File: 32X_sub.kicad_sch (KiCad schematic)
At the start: 103 parts, among them IC511 315-5684, IC512 315-5788, IC515 74HC74, IC516 74LS00, T520 TestPoint, T526 TestPoint, T527 TestPoint, T528 TestPoint, T547 TestPoint, T548 TestPoint, T555 TestPoint, T599 AS, X501 *3

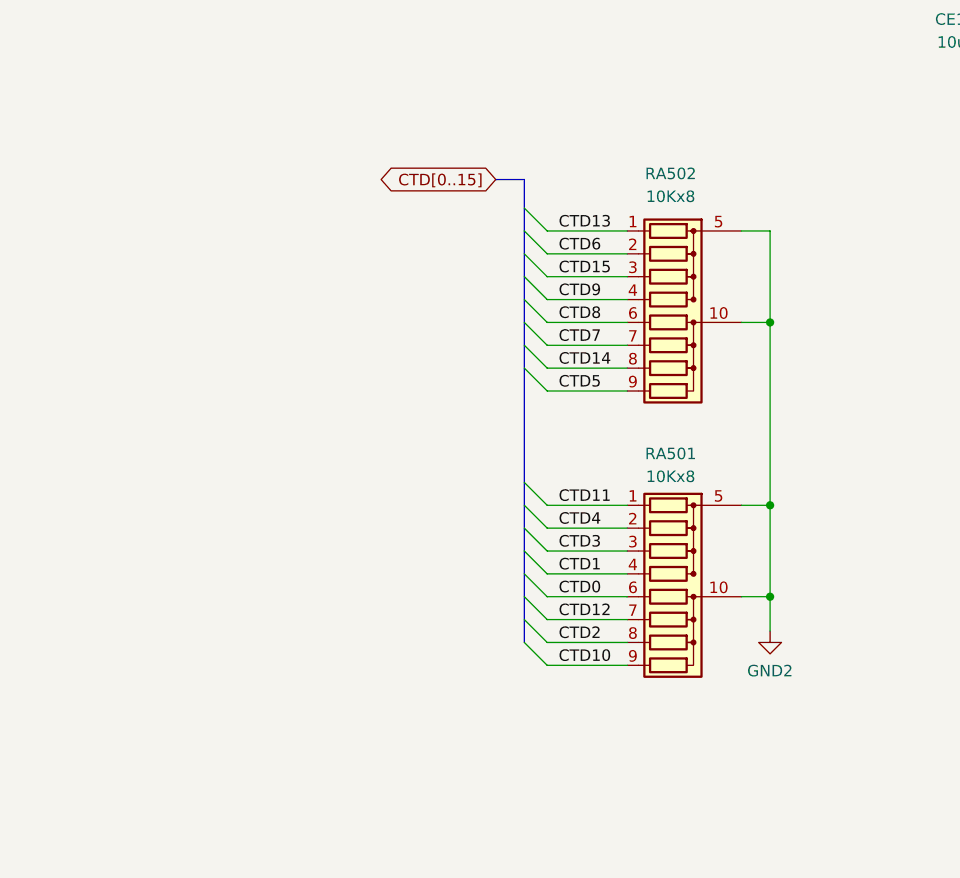
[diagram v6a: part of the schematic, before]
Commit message: Use more readily-available resistor packs.
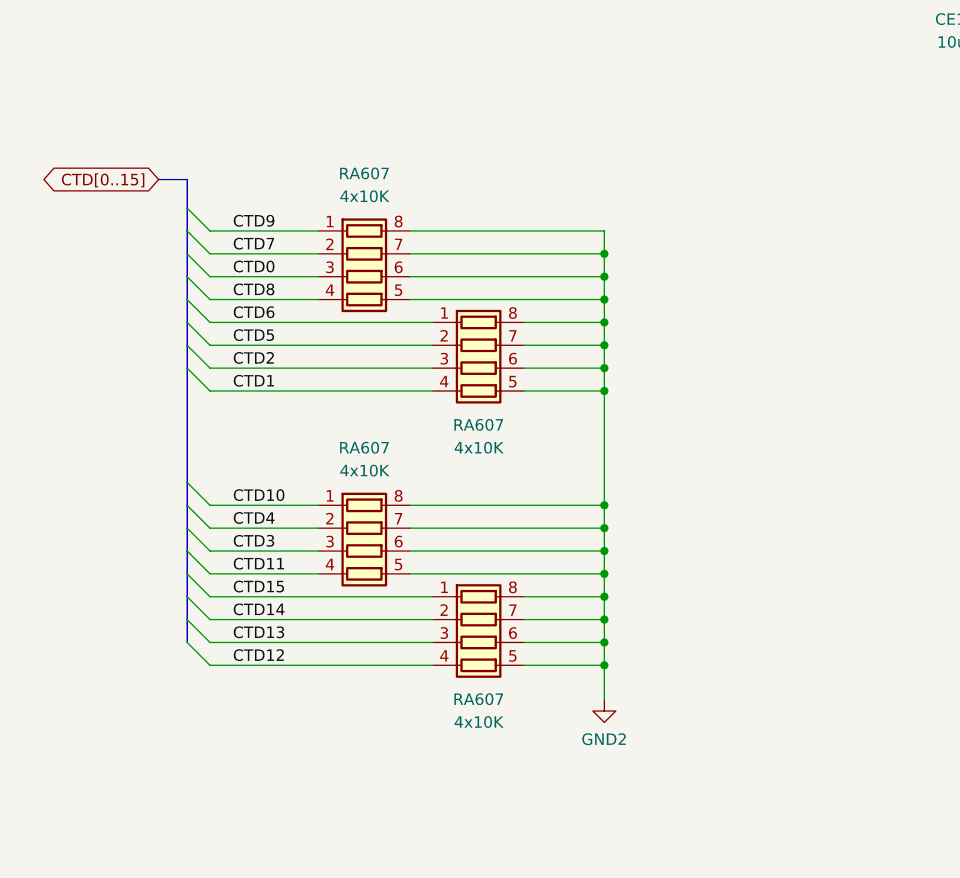
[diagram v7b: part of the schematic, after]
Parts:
- removed RA501, RA502: 10Kx8, Neptune:RA_8_2Common, symbol 32X:R_Network08_2Common
- added RA607 (x4): 4x10K, Resistor_SMD:R_Array_Convex_4x0603, symbol Device:R_Pack04
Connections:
- net CTD0: now also RA607.3 (R3.1)
- net CTD1: now also RA607.4 (R4.1)
- net CTD10: now also RA607.1 (R1.1)
- net CTD11: now also RA607.4 (R4.1)
- net CTD12: now also RA607.4 (R4.1)
- net CTD13: now also RA607.3 (R3.1)
- net CTD14: now also RA607.2 (R2.1)
- net CTD15: now also RA607.1 (R1.1)
- net CTD2: now also RA607.3 (R3.1)
- net CTD3: now also RA607.3 (R3.1)
- net CTD4: now also RA607.2 (R2.1)
- net CTD5: now also RA607.2 (R2.1)
- net CTD6: now also RA607.1 (R1.1)
- net CTD7: now also RA607.2 (R2.1)
- net CTD8: now also RA607.4 (R4.1)
- net CTD9: now also RA607.1 (R1.1)
- net GND2: now also RA607.5 (R4.2), RA607.5 (R4.2), RA607.5 (R4.2), RA607.5 (R4.2), RA607.6 (R3.2), RA607.6 (R3.2), RA607.6 (R3.2), RA607.6 (R3.2), RA607.7 (R2.2), RA607.7 (R2.2), RA607.7 (R2.2), RA607.7 (R2.2), RA607.8 (R1.2), RA607.8 (R1.2), RA607.8 (R1.2), RA607.8 (R1.2)

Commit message: Added resistor array parts
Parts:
- RA607: LCSC Part # (none) -> C110924; MPN (none) -> YC164-FR-0710KL
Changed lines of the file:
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@@
+      (effects (font (size 1.27 1.27)) hide)
+    )
+    (property "LCSC Part #" "C110924" (at 80.01 255.27 0)
+      (effects (font (size 1.27 1.27)) hide)
+    )
+    (property "MPN" "YC164-FR-0710KL" (at 80.01 255.27 0)
       (effects (font (size 1.27 1.27)) hide)
     )
@@
       (effects (font (size 1.27 1.27)) hide)
     )
+    (property "LCSC Part #" "C110924" (at 67.31 245.11 0)
+      (effects (font (size 1.27 1.27)) hide)
+    )
+    (property "MPN" "YC164-FR-0710KL" (at 67.31 245.11 0)
+      (effects (font (size 1.27 1.27)) hide)
+    )
     (pin "1")
     (pin "2")
@@
       (effects (font (size 1.27 1.27)) hide)
     )
+    (property "LCSC Part #" "C110924" (at 67.31 214.63 0)
+      (effects (font (size 1.27 1.27)) hide)
+    )
+    (property "MPN" "YC164-FR-0710KL" (at 67.31 214.63 0)
+      (effects (font (size 1.27 1.27)) hide)
+    )
     (pin "1")
     (pin "2")
@@
       (effects (font (size 1.27 1.27)) hide)
     )
+    (property "LCSC Part #" "C110924" (at 80.01 224.79 0)
+      (effects (font (size 1.27 1.27)) hide)
+    )
+    (property "MPN" "YC164-FR-0710KL" (at 80.01 224.79 0)
+      (effects (font (size 1.27 1.27)) hide)
+    )
